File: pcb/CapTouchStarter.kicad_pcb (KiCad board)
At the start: 4 copper layers, 76.5 x 66 mm, 59 parts, among them J1 USB_C_Receptacle, J2 Conn_ARM_JTAG_SWD_10, J3 62684-50110, Q1 SS8050-G, Q2 SS8050-G, SW1 SW_SPDT, SW2 EN, SW3 BOOT, U1 CP2102N-A01-GQFN28, U2 BD48K33G-TLCT-ND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

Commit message: Upgraded to KiCAD 6.
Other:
- net class Default removed

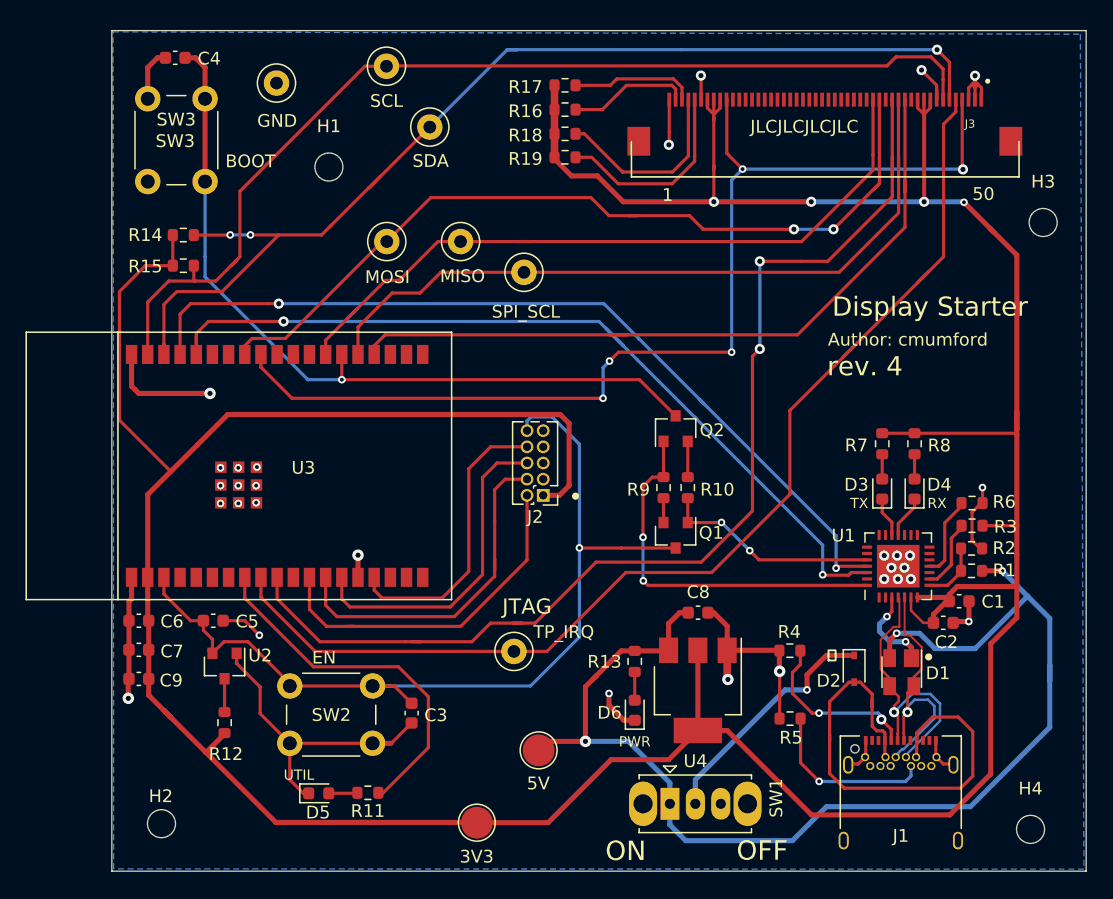
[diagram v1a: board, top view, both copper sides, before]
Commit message: Deleted unconnected tracks.
And one unnecessary via.
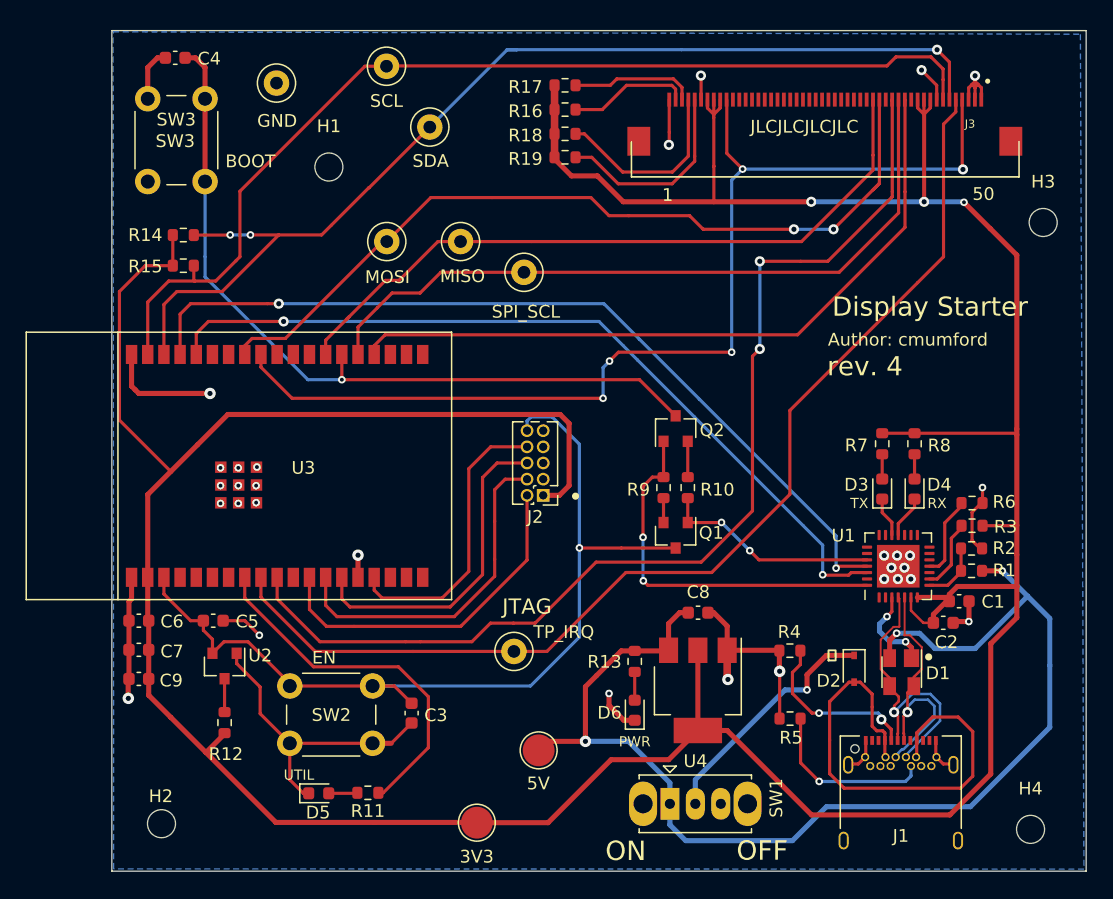
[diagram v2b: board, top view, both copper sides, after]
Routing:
- net +3V3: track 310.3 -> 304.0 mm, vias 4 -> 3
- net RXD: track 68.0 -> 64.4 mm
- net DC: track 87.7 -> 84.7 mm
- net CTP_IRQ: track 88.9 -> 86.4 mm
- net CTP_SDA: track 87.0 -> 84.7 mm
- net CS: track 58.5 -> 56.2 mm
- net MISO: track 57.9 -> 55.7 mm
- net VBUS: track 97.1 -> 95.4 mm
- net GND: track 107.0 -> 105.7 mm
- net SPI_SCL: track 58.3 -> 57.2 mm
- net Net-(D2-Pad2): track 39.6 -> 38.6 mm
- net JTAG_TCK: track 27.7 -> 26.8 mm
- net MOSI: track 65.9 -> 65.1 mm
- net TXD: track 68.2 -> 67.6 mm
- net CTP_SCL: track 82.2 -> 81.6 mm

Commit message: More DRC fixes.
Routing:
- net EN: track 72.7 -> 75.1 mm
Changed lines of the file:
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@@
       (effects (font (size 1 1) (thickness 0.15)))
     )
-    (fp_text value "68Ω" (at 5.842 -0.127) (layer "F.Fab")
+    (fp_text value "68Ω" (at 6.096 -0.3175) (layer "F.Fab")
       (effects (font (size 1 1) (thickness 0.15)))
     )
@@
       (effects (font (size 1 1) (thickness 0.15)))
     )
-    (fp_text value "68Ω" (at 5.842 0) (layer "F.Fab")
+    (fp_text value "68Ω" (at 6.096 -0.1905) (layer "F.Fab")
       (effects (font (size 1 1) (thickness 0.15)))
     )
@@
       (effects (font (size 1 1) (thickness 0.15)))
     )
-    (fp_text value "68Ω" (at 5.842 -0.0635) (layer "F.Fab")
+    (fp_text value "68Ω" (at 6.096 -0.254) (layer "F.Fab")
       (effects (font (size 1 1) (thickness 0.15)))
     )
@@
       (effects (font (size 1 1) (thickness 0.15)))
     )
-    (fp_text value "68Ω" (at 5.842 0) (layer "F.Fab")
+    (fp_text value "68Ω" (at 6.096 -0.1905) (layer "F.Fab")
       (effects (font (size 1 1) (thickness 0.15)))
     )
@@
       (effects (font (size 1 1) (thickness 0.15)))
     )
-    (fp_text value "BD48K33G-TLCT-ND" (at 4.064 -0.8255 180) (layer "F.Fab")
-      (effects (font (size 1 1) (thickness 0.15)))
+    (fp_text value "BD48K33G-TLCT-ND" (at 2.159 -0.0635 180) (layer "F.Fab")
+      (effects (font (size 0.3 0.3) (thickness 0.075)))
     )
     (fp_text user "${REFERENCE}" (at 0 0) (layer "F.Fab")
@@
     (tags "Through hole pin header THT 2x05 1.27mm double row")
     (attr through_hole)
-    (fp_text reference "J2" (at 0.635 -1.695) (layer "F.SilkS")
+    (fp_text reference "J2" (at 0.635 -2.0955) (layer "F.SilkS")
       (effects (font (size 1 1) (thickness 0.15)))
     )
@@
       (effects (font (size 1 1) (thickness 0.15)))
     )
-    (fp_text user "${REFERENCE}" (at 0.635 2.54 90) (layer "F.Fab")
+    (fp_text user "${REFERENCE}" (at 3.8735 4.7625 180) (layer "F.Fab")
       (effects (font (size 1 1) (thickness 0.15)))
     )
@@
   (segment (start 133.287 94.05366) (end 133.287 96.4565) (width 0.25) (layer "F.Cu") (net 2))
   (segment (start 191.246 123.53468) (end 192.21196 124.50064) (width 0.2) (layer "F.Cu") (net 2))
-  (segment (start 129.0955 98.4885) (end 131.1275 96.4565) (width 0.25) (layer "F.Cu") (net 2))
   (segment (start 175.7652 88.6488) (end 175.7652 84.8332) (width 0.25) (layer "F.Cu") (net 2))
   (segment (start 163.259 87.9475) (end 163.259 88.075) (width 0.25) (layer "F.Cu") (net 2))
@@
   (segment (start 131.3945 128.8415) (end 131.331 128.905) (width 0.4) (layer "F.Cu") (net 2))
   (segment (start 172.22256 135.24484) (end 174.51324 132.95416) (width 0.4) (layer "F.Cu") (net 2))
+  (segment (start 129.286 98.298) (end 129.667 97.917) (width 0.25) (layer "F.Cu") (net 2))
   (segment (start 199.55764 119.14632) (end 199.55764 121.64568) (width 0.4) (layer "F.Cu") (net 2))
   (segment (start 131.3945 126.619) (end 131.3945 128.8415) (width 0.4) (layer "F.Cu") (net 2))
@@
   (segment (start 191.7652 83.4202) (end 191.7652 84.0692) (width 0.25) (layer "F.Cu") (net 2))
   (segment (start 199.55764 109.28096) (end 199.55764 95.631) (width 0.4) (layer "F.Cu") (net 2))
+  (segment (start 129.286 108.7755) (end 129.286 98.298) (width 0.25) (layer "F.Cu") (net 2))
   (segment (start 141.37894 140.17244) (end 149.12594 140.17244) (width 0.4) (layer "F.Cu") (net 2))
   (segment (start 157.15996 140.19276) (end 162.75304 140.19276) (width 0.4) (layer "F.Cu") (net 2))
@@
   (segment (start 131.3945 128.905) (end 131.3945 130.188) (width 0.4) (layer "F.Cu") (net 2))
   (segment (start 131.318 114.427) (end 131.318 120.9291) (width 0.4) (layer "F.Cu") (net 2))
-  (segment (start 133.12775 112.61725) (end 129.0955 108.585) (width 0.25) (layer "F.Cu") (net 2))
   (segment (start 175.2652 83.4202) (end 175.2652 84.0792) (width 0.25) (layer "F.Cu") (net 2))
   (segment (start 199.55764 95.631) (end 197.47484 93.5482) (width 0.4) (layer "F.Cu") (net 2))
@@
   (segment (start 133.12775 112.61725) (end 131.318 114.427) (width 0.4) (layer "F.Cu") (net 2))
   (segment (start 137.3505 133.223) (end 135.89 134.6835) (width 0.4) (layer "F.Cu") (net 2))
+  (segment (start 129.667 97.917) (end 131.1275 96.4565) (width 0.25) (layer "F.Cu") (net 2))
   (segment (start 199.55764 121.64568) (end 199.55764 124.08916) (width 0.4) (layer "F.Cu") (net 2))
   (segment (start 194.87896 121.64568) (end 199.55764 121.64568) (width 0.4) (layer "F.Cu") (net 2))
   (segment (start 163.6395 114.4905) (end 164.4015 113.7285) (width 0.4) (layer "F.Cu") (net 2))
   (segment (start 199.4286 109.6142) (end 199.55764 109.74324) (width 0.25) (layer "F.Cu") (net 2))
-  (segment (start 129.0955 108.585) (end 129.0955 98.4885) (width 0.25) (layer "F.Cu") (net 2))
+  (segment (start 133.12775 112.61725) (end 129.286 108.7755) (width 0.25) (layer "F.Cu") (net 2))
   (segment (start 175.7652 83.4202) (end 175.7652 84.5792) (width 0.25) (layer "F.Cu") (net 2))
   (segment (start 163.259 82.296) (end 163.259 84.201) (width 0.6) (layer "F.Cu") (net 2))
@@
   (segment (start 139.192 125.984) (end 142.471 129.263) (width 0.25) (layer "F.Cu") (net 14))
   (via (at 165.21176 118.618) (size 0.6) (drill 0.3) (layers "F.Cu" "B.Cu") (net 14))
-  (segment (start 165.21176 110.47476) (end 165.21176 121.92508) (width 0.25) (layer "B.Cu") (net 14))
-  (segment (start 161.0995 109.4105) (end 161.0995 108.6485) (width 0.25) (layer "B.Cu") (net 14))
-  (segment (start 163.068 108.331) (end 165.21176 110.47476) (width 0.25) (layer "B.Cu") (net 14))
-  (segment (start 148.971 129.4596) (end 161.3704 129.4596) (width 0.25) (layer "B.Cu") (net 14))
-  (segment (start 161.417 108.331) (end 163.068 108.331) (width 0.25) (layer "B.Cu") (net 14))
-  (segment (start 161.0995 108.6485) (end 161.417 108.331) (width 0.25) (layer "B.Cu") (net 14))
-  (segment (start 161.3704 129.4596) (end 165.21176 125.61824) (width 0.25) (layer "B.Cu") (net 14))
-  (segment (start 165.21176 125.61824) (end 165.21176 121.92508) (width 0.25) (layer "B.Cu") (net 14))
+  (segment (start 165.21176 108.31576) (end 165.21176 125.61824) (width 0.25) (layer "B.Cu") (net 14))
+  (segment (start 164.338 107.442) (end 165.21176 108.31576) (width 0.25) (layer "B.Cu") (net 14))
+  (segment (start 161.544 107.442) (end 164.338 107.442) (width 0.25) (layer "B.Cu") (net 14))
+  (segment (start 165.21176 125.61824) (end 161.3704 129.4596) (width 0.25) (layer "B.Cu") (net 14))
+  (segment (start 161.3704 129.4596) (end 148.971 129.4596) (width 0.25) (layer "B.Cu") (net 14))
+  (segment (start 161.0995 107.8865) (end 161.544 107.442) (width 0.25) (layer "B.Cu") (net 14))
+  (segment (start 161.0995 109.4105) (end 161.0995 107.8865) (width 0.25) (layer "B.Cu") (net 14))
   (segment (start 190.22166 131.81612) (end 189.92166 131.51612) (width 0.2) (layer "F.Cu") (net 15))
   (segment (start 190.19666 133.73512) (end 190.19666 133.210119) (width 0.2) (layer "F.Cu") (net 15))

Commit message: Switched to KiCAD 6 CP2102N symbol.
It looks like the v5 CP2102N-A01-GQFN28 symbol was renamed
to CP2102N-Axx-xQFN28 in v6.
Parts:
- U1: value CP2102N-A01-GQFN28 -> CP2102N-Axx-xQFN28
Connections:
- D1 pad 3: D+ -> D-
- D1 pad 4: D- -> D+
- J1 pad A10: Net-(J1-PadA10) -> unconnected-(J1-PadA10)
- J1 pad A11: Net-(J1-PadA11) -> unconnected-(J1-PadA11)
- J1 pad A2: Net-(J1-PadA2) -> unconnected-(J1-PadA2)
- J1 pad A3: Net-(J1-PadA3) -> unconnected-(J1-PadA3)
- J1 pad A8: Net-(J1-PadA8) -> unconnected-(J1-PadA8)
- J1 pad B10: Net-(J1-PadB10) -> unconnected-(J1-PadB10)
- J1 pad B11: Net-(J1-PadB11) -> unconnected-(J1-PadB11)
- J1 pad B2: Net-(J1-PadB2) -> unconnected-(J1-PadB2)
- J1 pad B3: Net-(J1-PadB3) -> unconnected-(J1-PadB3)
- J1 pad B8: Net-(J1-PadB8) -> unconnected-(J1-PadB8)
- J2 pad 7: Net-(J2-Pad7) -> unconnected-(J2-Pad7)
- J3 pad 12: Net-(J3-Pad12) -> unconnected-(J3-Pad12)
- J3 pad 16: Net-(J3-Pad16) -> unconnected-(J3-Pad16)
- J3 pad 19: Net-(J3-Pad19) -> unconnected-(J3-Pad19)
- J3 pad 20: Net-(J3-Pad20) -> unconnected-(J3-Pad20)
- J3 pad 21: Net-(J3-Pad21) -> unconnected-(J3-Pad21)
- J3 pad 22: Net-(J3-Pad22) -> unconnected-(J3-Pad22)
- J3 pad 23: Net-(J3-Pad23) -> unconnected-(J3-Pad23)
- J3 pad 24: Net-(J3-Pad24) -> unconnected-(J3-Pad24)
- J3 pad 25: Net-(J3-Pad25) -> unconnected-(J3-Pad25)
- J3 pad 26: Net-(J3-Pad26) -> unconnected-(J3-Pad26)
- J3 pad 27: Net-(J3-Pad27) -> unconnected-(J3-Pad27)
- J3 pad 28: Net-(J3-Pad28) -> unconnected-(J3-Pad28)
- J3 pad 29: Net-(J3-Pad29) -> unconnected-(J3-Pad29)
- J3 pad 30: Net-(J3-Pad30) -> unconnected-(J3-Pad30)
- J3 pad 31: Net-(J3-Pad31) -> unconnected-(J3-Pad31)
- J3 pad 32: Net-(J3-Pad32) -> unconnected-(J3-Pad32)
- J3 pad 33: Net-(J3-Pad33) -> unconnected-(J3-Pad33)
- J3 pad 34: Net-(J3-Pad34) -> unconnected-(J3-Pad34)
- J3 pad 35: Net-(J3-Pad35) -> unconnected-(J3-Pad35)
- J3 pad 36: Net-(J3-Pad36) -> unconnected-(J3-Pad36)
- J3 pad 37: Net-(J3-Pad37) -> unconnected-(J3-Pad37)
- J3 pad 38: Net-(J3-Pad38) -> unconnected-(J3-Pad38)
- J3 pad 39: Net-(J3-Pad39) -> unconnected-(J3-Pad39)
- J3 pad 40: Net-(J3-Pad40) -> unconnected-(J3-Pad40)
- SW1 pad 3: Net-(SW1-Pad3) -> unconnected-(SW1-Pad3)
- U1 pad 1: Net-(U1-Pad1) -> unconnected-(U1-Pad1)
- U1 pad 10: Net-(U1-Pad10) -> unconnected-(U1-Pad10)
- U1 pad 12: Net-(U1-Pad12) -> unconnected-(U1-Pad12)
- U1 pad 13: Net-(U1-Pad13) -> unconnected-(U1-Pad13)
- U1 pad 14: Net-(U1-Pad14) -> unconnected-(U1-Pad14)
- U1 pad 15: Net-(U1-Pad15) -> unconnected-(U1-Pad15)
- U1 pad 16: Net-(U1-Pad16) -> unconnected-(U1-Pad16)
- U1 pad 17: Net-(U1-Pad17) -> unconnected-(U1-Pad17)
- U1 pad 2: Net-(U1-Pad2) -> unconnected-(U1-Pad2)
- U1 pad 20: Net-(U1-Pad20) -> unconnected-(U1-Pad20)
- U1 pad 21: Net-(U1-Pad21) -> unconnected-(U1-Pad21)
- U1 pad 22: Net-(U1-Pad22) -> unconnected-(U1-Pad22)
- U1 pad 23: Net-(U1-Pad23) -> unconnected-(U1-Pad23)
- U1 pad 27: Net-(U1-Pad27) -> unconnected-(U1-Pad27)
- U3 pad 11: Net-(U3-Pad11) -> unconnected-(U3-Pad11)
- U3 pad 17: Net-(U3-Pad17) -> unconnected-(U3-Pad17)
- U3 pad 18: Net-(U3-Pad18) -> unconnected-(U3-Pad18)
- U3 pad 19: Net-(U3-Pad19) -> unconnected-(U3-Pad19)
- U3 pad 20: Net-(U3-Pad20) -> unconnected-(U3-Pad20)
- U3 pad 21: Net-(U3-Pad21) -> unconnected-(U3-Pad21)
- U3 pad 22: Net-(U3-Pad22) -> unconnected-(U3-Pad22)
- U3 pad 27: Net-(U3-Pad27) -> unconnected-(U3-Pad27)
- U3 pad 28: Net-(U3-Pad28) -> unconnected-(U3-Pad28)
- U3 pad 29: Net-(U3-Pad29) -> unconnected-(U3-Pad29)
- U3 pad 32: Net-(U3-Pad32) -> unconnected-(U3-Pad32)
- U3 pad 33: Net-(U3-Pad33) -> unconnected-(U3-Pad33)
- U3 pad 4: Net-(U3-Pad4) -> unconnected-(U3-Pad4)
- U3 pad 5: Net-(U3-Pad5) -> unconnected-(U3-Pad5)
- U3 pad 6: Net-(U3-Pad6) -> unconnected-(U3-Pad6)
- U3 pad 7: Net-(U3-Pad7) -> unconnected-(U3-Pad7)

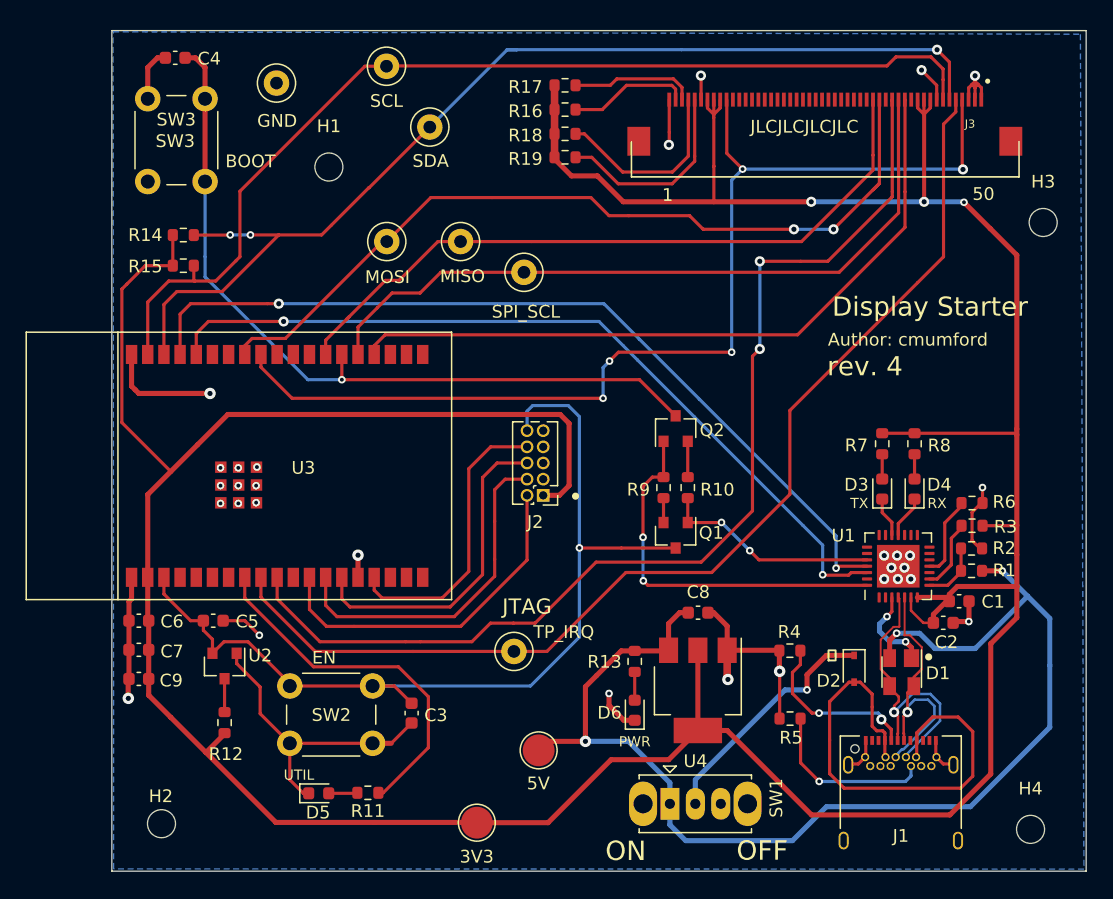
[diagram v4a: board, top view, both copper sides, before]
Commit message: Cleanup and IO0 route fix.
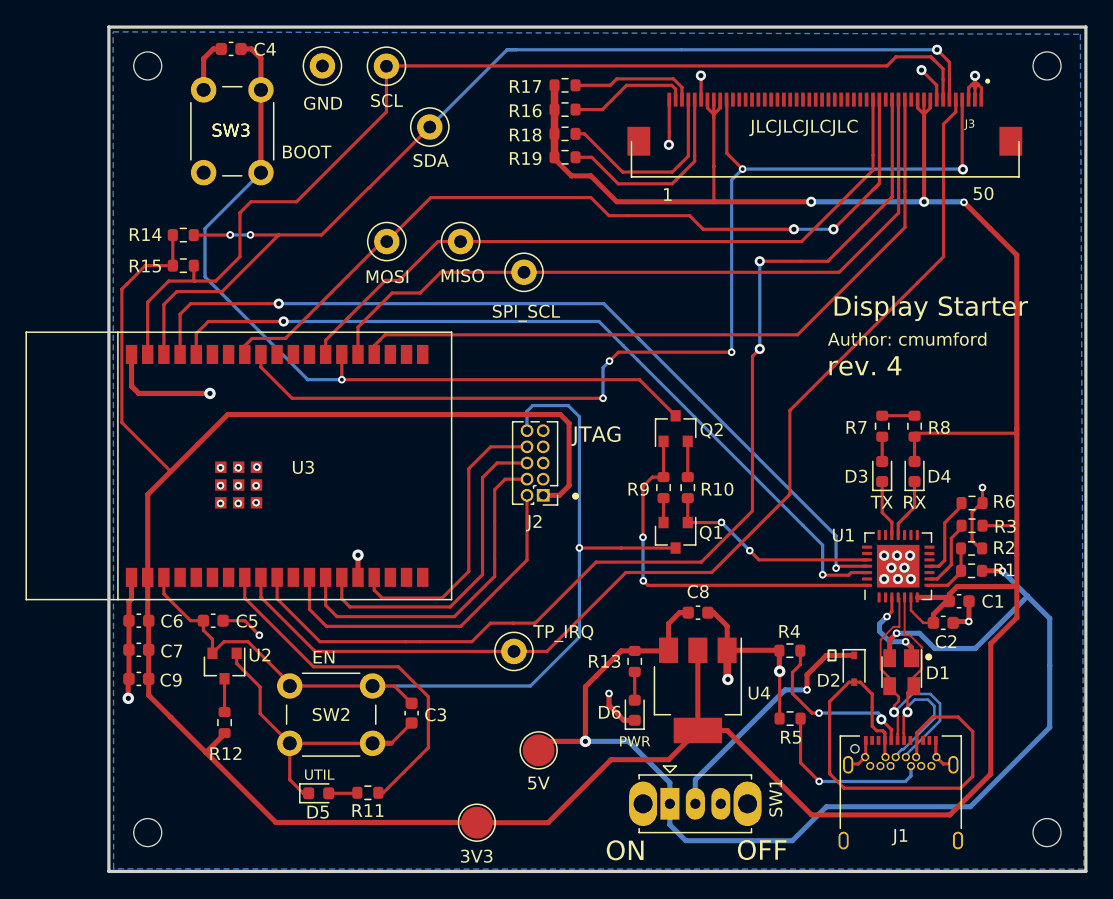
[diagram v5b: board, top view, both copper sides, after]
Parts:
- moved H1 16.3 mm to (131.3, 80.8)
- moved H3 12.3 mm to (201.9, 80.8)
- moved SW3 4.45 mm to (135.7, 89.2)
- moved C4 4.45 mm to (137.9, 79.4)
- moved TP2 3.85 mm to (145.0, 80.8)
- moved D3 1.38 mm to (189.0, 112.6)
- moved D4 1.38 mm to (191.5, 112.6)
- moved R7 1.38 mm to (189.0, 109.1)
- moved R8 1.38 mm to (191.5, 109.1)
- moved H4 1.32 mm to (201.9, 141.0)
- moved H2 1.29 mm to (131.3, 141.0)
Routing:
- net IO0: track 61.8 -> 64.3 mm
- net Net-(D3-Pad1): track 3.14 -> 4.51 mm
- net Net-(D4-Pad1): track 3.35 -> 4.73 mm
- net CTP_SCL: track 81.6 -> 82.8 mm
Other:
- board size 76.5 x 66 mm -> 76.7 x 66.3 mm
